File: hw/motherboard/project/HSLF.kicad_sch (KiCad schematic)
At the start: 76 parts, among them J1 JST_01x02_Pin, J2 Conn_01x12_Pin, J3 JST_01x02_Pin, J4 JST_01x02_Pin, J5 IDC_Conn_STLink-V2, J6 USB4940-00-A, J7 XT60-M, Q1 Q_NMOS_DGS, Q2 AO3401A, SW1 SW_Push, SW2 SW_Push, SW3 SW_SPDT, U1 STM32F103C8T6, U2 TPS563201, U3 AMS1117-5.0, U4 VS1838B, U5 A4950E, U6 A4950E, Y1 16MHz

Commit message: the assignment of footprints and 3D models has been completed
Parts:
- C10, C11, C12, C13, C14, C15, C16, C17, C18, C20, C22, C23, C25, C26, C3, C4, C5, C6, C7, C8, C9: footprint (none) -> Capacitor_SMD:C_0805_2012Metric_Pad1.18x1.45mm_HandSolder
- C19: footprint (none) -> Capacitor_SMD:CP_Elec_5x3
- C21, C24: footprint (none) -> Capacitor_SMD:CP_Elec_6.3x5.4
- D1, D2, D3, D4, D5: footprint (none) -> LED_SMD:LED_1206_3216Metric_Pad1.42x1.75mm_HandSolder
- J1, J3, J4: footprint (none) -> Connector_JST:JST_XH_B2B-XH-A_1x02_P2.50mm_Vertical
- J2: footprint (none) -> Connector_JST:JST_XH_B12B-XH-A_1x12_P2.50mm_Vertical
- J5: footprint (none) -> Connector_IDC:IDC-Header_2x05_P2.54mm_Vertical
- J6: footprint USB494000A -> HSLF:USB494000A
- J7: footprint (none) -> Connector_AMASS:AMASS_XT60-M_1x02_P7.20mm_Vertical
- L1: footprint (none) -> Inductor_SMD:L_APV_APH0618
- Q1: footprint (none) -> Package_TO_SOT_SMD:TSOT-23_HandSoldering
- R1, R10, R11, R12, R13, R14, R15, R16, R17, R18, R19, R2, R20, R21, R22, R3, R4, R5, R6, R7, R8, R9: footprint (none) -> Resistor_SMD:R_0805_2012Metric_Pad1.20x1.40mm_HandSolder
- SW1, SW2: footprint (none) -> Button_Switch_SMD:SW_Push_1P1T_NO_E-Switch_TL3301NxxxxxG
- SW3: footprint (none) -> Button_Switch_THT:SW_Slide_SPDT_Straight_CK_OS102011MS2Q
- TP1, TP2, TP3: footprint (none) -> TestPoint:TestPoint_Pad_1.0x1.0mm
- Y1: footprint (none) -> Crystal:Crystal_SMD_3225-4Pin_3.2x2.5mm_HandSoldering

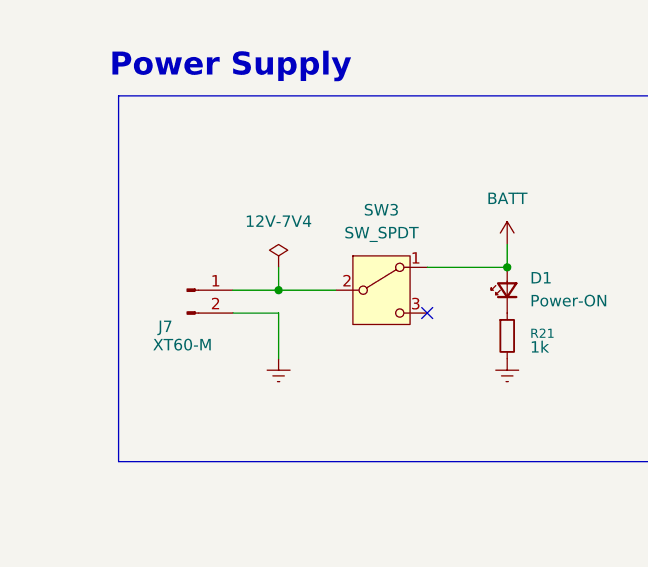
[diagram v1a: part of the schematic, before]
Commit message: Add design layout motherboard
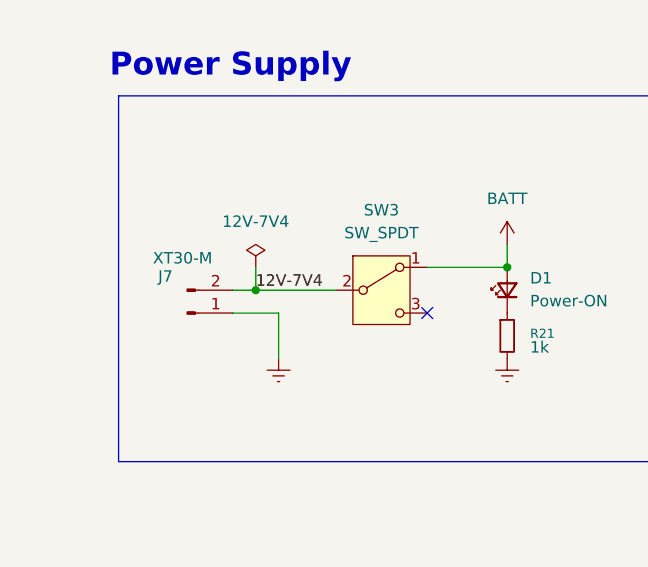
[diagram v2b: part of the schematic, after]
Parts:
- D6, D7: footprint Diode_THT:D_DO-41_SOD81_P10.16mm_Horizontal -> Diode_SMD:D_1206_3216Metric_Pad1.42x1.75mm_HandSolder
- J7: value XT60-M -> XT30-M; footprint Connector_AMASS:AMASS_XT60-M_1x02_P7.20mm_Vertical -> Connector_AMASS:AMASS_XT30UPB-M_1x02_P5.0mm_Vertical
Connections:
- net GND: now also J7.1 (Pin_1); no longer J7.2 (Pin_2)
- net 12V-7V4: now reaches SW3.2 (B)
- net 12V-7V4: now also J7.2 (Pin_2); no longer J7.1 (Pin_1)
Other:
- company: Kauê Lucas Nascimento da Silva & Laio -> Kauê Lucas & Vicente Laio
- title: HSFL MotherBoard -> HSFL MotherBoard Schematic
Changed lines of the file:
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@@
 	(paper "A3")
 	(title_block
-		(title "HSFL MotherBoard")
+		(title "HSFL MotherBoard Schematic")
 		(date "2026-07-16")
 		(rev "1.1")
-		(company "Kauê Lucas Nascimento da Silva & Laio")
+		(company "Kauê Lucas & Vicente Laio")
 	)
 	(rectangle
@@
 	)
 	(junction
-		(at 39.37 46.99)
-		(diameter 0)
-		(color 0 0 0 0)
-	)
-	(junction
 		(at 31.75 115.57)
 		(diameter 0)
@@
 	)
 	(junction
+		(at 36.83 46.99)
+		(diameter 0)
+		(color 0 0 0 0)
+	)
+	(junction
 		(at 101.6 100.33)
 		(diameter 0)
@@
 	(wire
 		(pts
-			(xy 39.37 46.99) (xy 45.72 46.99)
-		)
-		(stroke
-			(width 0)
-			(type default)
-		)
-	)
-	(wire
-		(pts
 			(xy 83.82 152.4) (xy 91.44 152.4)
 		)
@@
 	(wire
 		(pts
-			(xy 34.29 46.99) (xy 39.37 46.99)
+			(xy 34.29 46.99) (xy 36.83 46.99)
 		)
 		(stroke
@@
 	(wire
 		(pts
+			(xy 36.83 46.99) (xy 45.72 46.99)
+		)
+		(stroke
+			(width 0)
+			(type default)
+		)
+	)
+	(wire
+		(pts
 			(xy 154.94 153.67) (xy 154.94 158.75)
 		)
@@
 	(wire
 		(pts
-			(xy 39.37 44.45) (xy 39.37 46.99)
+			(xy 36.83 44.45) (xy 36.83 46.99)
 		)
 		(stroke
@@
 		)
 	)
+	(label "12V-7V4"
+		(at 36.83 46.99 0)
+		(effects
+			(font
+				(size 1.27 1.27)
+			)
+			(justify left bottom)
+		)
+	)
 	(label "Conn_USBC_D+"
 		(at 273.05 146.05 0)
@@
 	(symbol
 		(lib_id "power:PWR_FLAG")
-		(at 39.37 44.45 0)
+		(at 36.83 44.45 0)
 		(unit 1)
 		(body_style 1)
@@
 		(fields_autoplaced yes)
 		(property "Reference" "#FLG05"
-			(at 39.37 42.545 0)
+			(at 36.83 42.545 0)
 			(hide yes)
 			(show_name no)
@@
 		)
 		(property "Value" "12V-7V4"
-			(at 39.37 39.37 0)
+			(at 36.83 39.37 0)
 			(show_name no)
 			(do_not_autoplace no)
@@
 		)
 		(property "Footprint" ""
-			(at 39.37 44.45 0)
+			(at 36.83 44.45 0)
 			(hide yes)
 			(show_name no)
@@
 		)
 		(property "Datasheet" ""
-			(at 39.37 44.45 0)
+			(at 36.83 44.45 0)
 			(hide yes)
 			(show_name no)
@@
 		)
 		(property "Description" "Special symbol for telling ERC where power comes from"
-			(at 39.37 44.45 0)
+			(at 36.83 44.45 0)
 			(hide yes)
 			(show_name no)
@@
 	(symbol
 		(lib_id "Connector:Conn_01x02_Pin")
-		(at 29.21 46.99 0)
+		(at 29.21 49.53 0)
+		(mirror x)
 		(unit 1)
 		(body_style 1)
@@
 		(dnp no)
 		(property "Reference" "J7"
-			(at 26.797 51.054 0)
+			(at 26.797 45.466 0)
 			(show_name no)
 			(do_not_autoplace no)
@@
 			)
 		)
-		(property "Value" "XT60-M"
-			(at 28.702 53.086 0)
+		(property "Value" "XT30-M"
+			(at 28.702 43.434 0)
 			(show_name no)
 			(do_not_autoplace no)
@@
 			)
 		)
-		(property "Footprint" "Connector_AMASS:AMASS_XT60-M_1x02_P7.20mm_Vertical"
-			(at 29.21 46.99 0)
+		(property "Footprint" "Connector_AMASS:AMASS_XT30UPB-M_1x02_P5.0mm_Vertical"
+			(at 29.21 49.53 0)
 			(hide yes)
 			(show_name no)
@@
 		)
 		(property "Datasheet" ""
-			(at 29.21 46.99 0)
+			(at 29.21 49.53 0)
 			(hide yes)
 			(show_name no)
@@
 		)
 		(property "Description" "Generic connector, single row, 01x02, script generated"
-			(at 29.21 46.99 0)
+			(at 29.21 49.53 0)
 			(hide yes)
 			(show_name no)
@@
 			)
 		)
-		(property "Footprint" "Diode_THT:D_DO-41_SOD81_P10.16mm_Horizontal"
+		(property "Footprint" "Diode_SMD:D_1206_3216Metric_Pad1.42x1.75mm_HandSolder"
 			(at 76.2 146.685 0)
 			(hide yes)
@@
 			)
 		)
-		(property "Footprint" "Diode_THT:D_DO-41_SOD81_P10.16mm_Horizontal"
+		(property "Footprint" "Diode_SMD:D_1206_3216Metric_Pad1.42x1.75mm_HandSolder"
 			(at 141.605 43.18 0)
 			(hide yes)
